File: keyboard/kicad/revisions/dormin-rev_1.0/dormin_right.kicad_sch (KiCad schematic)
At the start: 116 parts, among them J4 Conn_01x06, J5 Conn_01x04, J6 Conn_01x04, Q3 AO3407A, Q4 AO3400A, SW21 SW_Push, SW22 SW_Push, SW23 SW_Push, SW24 SW_Push, SW25 SW_Push, SW26 SW_Push, SW27 SW_Push, SW28 SW_Push, SW29 SW_Push, SW30 SW_Push, SW31 SW_Push, SW32 SW_Push, SW33 SW_Push, SW34 SW_Push, SW35 SW_Push, SW36 SW_Push, SW37 SW_Push, SW38 SW_Push, SW39 SW_Push, SW40 SW_Push, U5 XIAO-nRF52840-Plus-SMD, U6 TPD2E2U06DCK

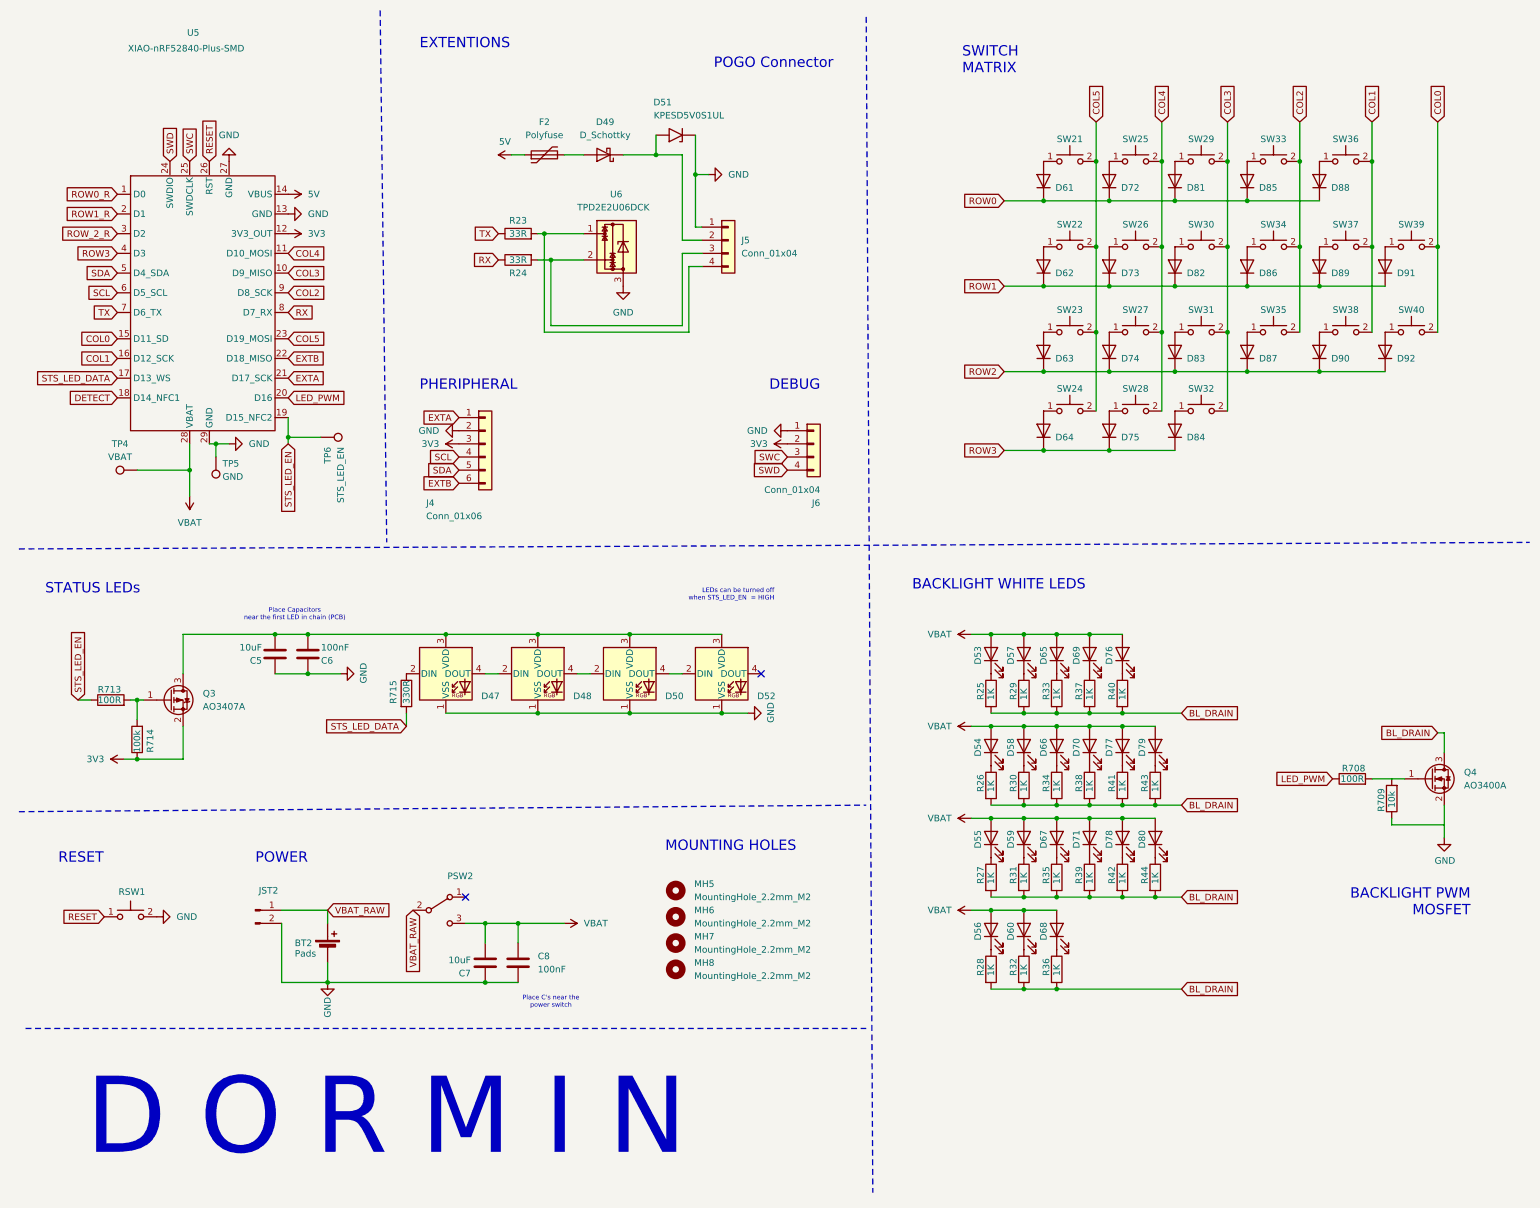
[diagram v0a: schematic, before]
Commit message: chore: update reference names for the right schematic
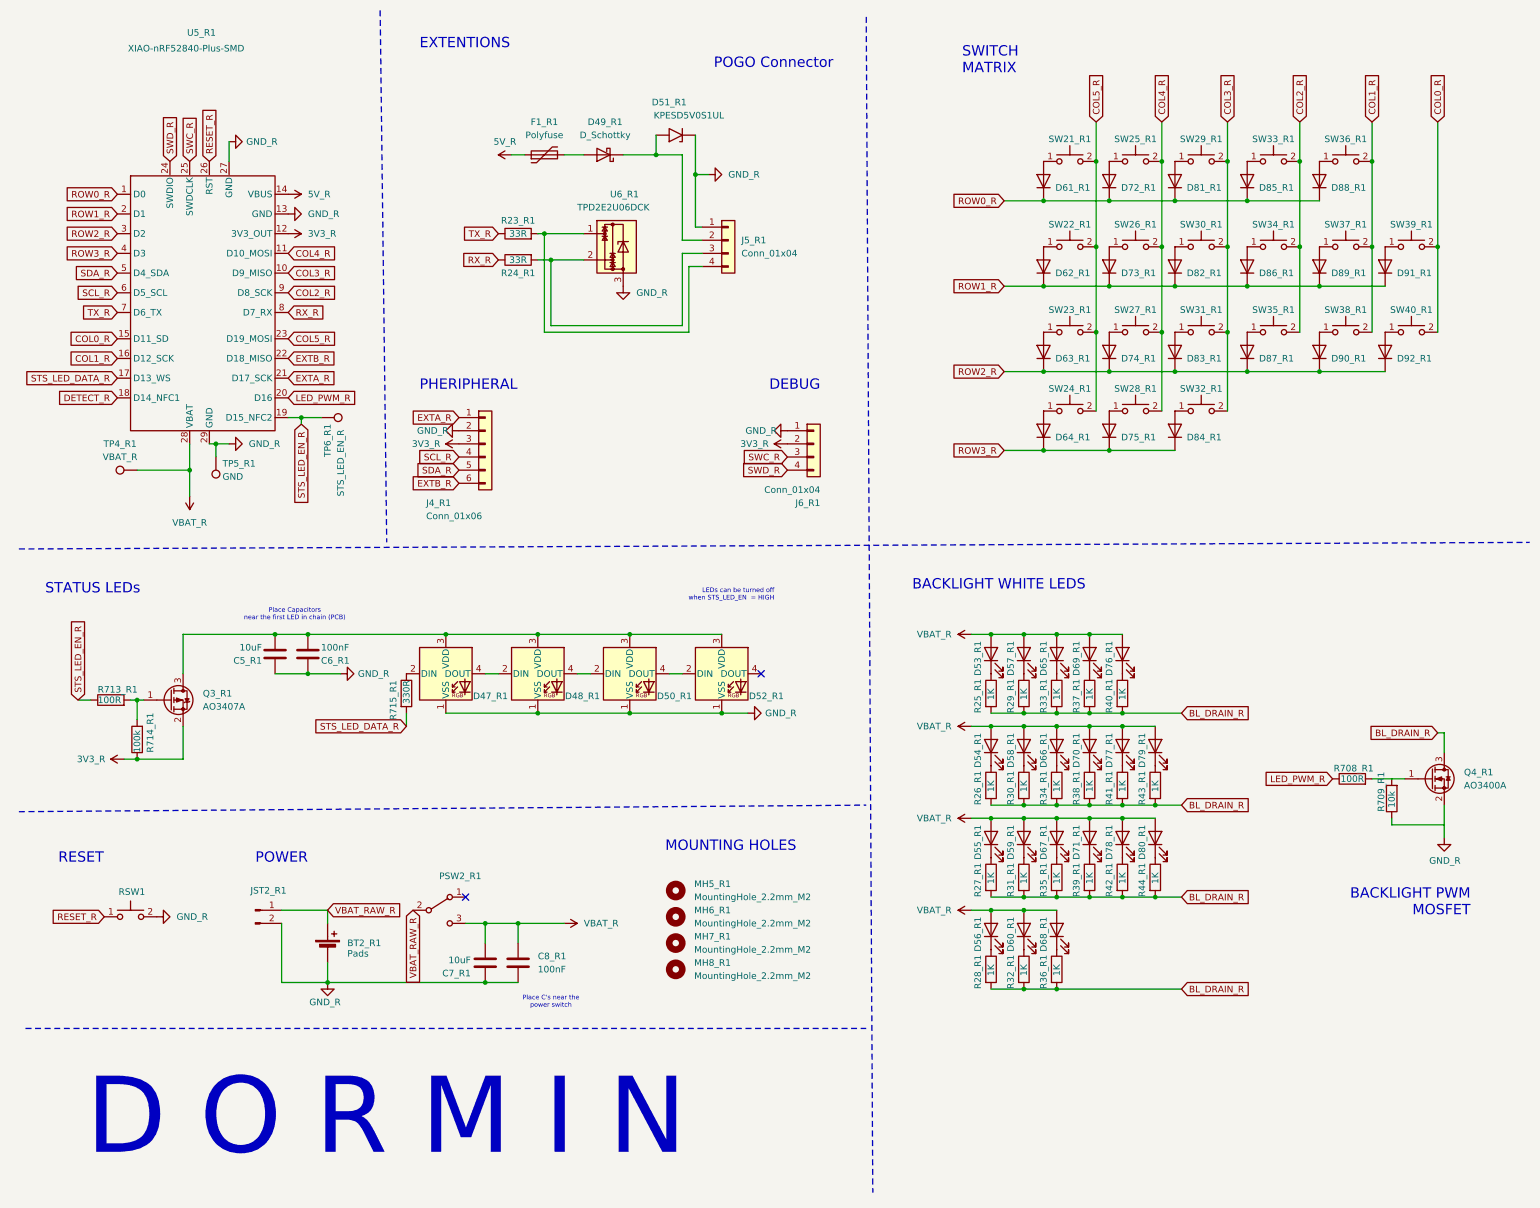
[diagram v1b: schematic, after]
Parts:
- TP4_R1: renamed from TP4; value VBAT -> VBAT_R
- TP6_R1: renamed from TP6; value STS_LED_EN -> STS_LED_EN_R
- renumbered BT2 to BT2_R1, C5 to C5_R1, C6 to C6_R1, C7 to C7_R1, C8 to C8_R1, D47 to D47_R1, D48 to D48_R1, D49 to D49_R1, D50 to D50_R1, D51 to D51_R1, D52 to D52_R1, D53 to D53_R1, D54 to D54_R1, D55 to D55_R1, D56 to D56_R1, D57 to D57_R1, D58 to D58_R1, D59 to D59_R1, D60 to D60_R1, D61 to D61_R1, D62 to D62_R1, D63 to D63_R1, D64 to D64_R1, D65 to D65_R1, D66 to D66_R1, D67 to D67_R1, D68 to D68_R1, D69 to D69_R1, D70 to D70_R1, D71 to D71_R1, D72 to D72_R1, D73 to D73_R1, D74 to D74_R1, D75 to D75_R1, D76 to D76_R1, D77 to D77_R1, D78 to D78_R1, D79 to D79_R1, D80 to D80_R1, D81 to D81_R1, D82 to D82_R1, D83 to D83_R1, D84 to D84_R1, D85 to D85_R1, D86 to D86_R1, D87 to D87_R1, D88 to D88_R1, D89 to D89_R1, D90 to D90_R1, D91 to D91_R1, D92 to D92_R1, F2 to F1_R1, J4 to J4_R1, J5 to J5_R1, J6 to J6_R1, JST2 to JST2_R1, MH5 to MH5_R1, MH6 to MH6_R1, MH7 to MH7_R1, MH8 to MH8_R1, PSW2 to PSW2_R1, Q3 to Q3_R1, Q4 to Q4_R1, R23 to R23_R1, R24 to R24_R1, R25 to R25_R1, R26 to R26_R1, R27 to R27_R1, R28 to R28_R1, R29 to R29_R1, R30 to R30_R1, R31 to R31_R1, R32 to R32_R1, R33 to R33_R1, R34 to R34_R1, R35 to R35_R1, R36 to R36_R1, R37 to R37_R1, R38 to R38_R1, R39 to R39_R1, R40 to R40_R1, R41 to R41_R1, R42 to R42_R1, R43 to R43_R1, R44 to R44_R1, R708 to R708_R1, R709 to R709_R1, R713 to R713_R1, R714 to R714_R1, R715 to R715_R1, RSW2 to RSW2_R1, SW21 to SW21_R1, SW22 to SW22_R1, SW23 to SW23_R1, SW24 to SW24_R1, SW25 to SW25_R1, SW26 to SW26_R1, SW27 to SW27_R1, SW28 to SW28_R1, SW29 to SW29_R1, SW30 to SW30_R1, SW31 to SW31_R1, SW32 to SW32_R1, SW33 to SW33_R1, SW34 to SW34_R1, SW35 to SW35_R1, SW36 to SW36_R1, SW37 to SW37_R1, SW38 to SW38_R1, SW39 to SW39_R1, SW40 to SW40_R1, TP5 to TP5_R1, U5 to U5_R1, U6 to U6_R1
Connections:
- net ROW0 is gone; now on net ROW0_R: D61_R1.1 (K), D72_R1.1 (K), D81_R1.1 (K), D85_R1.1 (K), D88_R1.1 (K)
- net ROW1 is gone; now on net ROW1_R: D62_R1.1 (K), D73_R1.1 (K), D82_R1.1 (K), D86_R1.1 (K), D89_R1.1 (K), D91_R1.1 (K)
- net ROW_2_R is gone; now on net ROW2_R: U5_R1.3 (D2)
- net 3V3 renamed 3V3_R
- net 5V renamed 5V_R
- net BL_DRAIN renamed BL_DRAIN_R
- net COL0 renamed COL0_R
- net COL1 renamed COL1_R
- net COL2 renamed COL2_R
- net COL3 renamed COL3_R
- net COL4 renamed COL4_R
- net COL5 renamed COL5_R
- net DETECT renamed DETECT_R
- net EXTA renamed EXTA_R
- net EXTB renamed EXTB_R
- net GND renamed GND_R
- net LED_PWM renamed LED_PWM_R
- net RESET renamed RESET_R
- net ROW2 renamed ROW2_R
- net ROW3 renamed ROW3_R
- net RX renamed RX_R
- net SCL renamed SCL_R
- net SDA renamed SDA_R
- net STS_LED_DATA renamed STS_LED_DATA_R
- net STS_LED_EN renamed STS_LED_EN_R
- net SWC renamed SWC_R
- net SWD renamed SWD_R
- net TX renamed TX_R
- net VBAT renamed VBAT_R
- net VBAT_RAW renamed VBAT_RAW_R
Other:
- moved on the sheet: TP6_R1

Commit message: feat: updated pogo-pin schematics
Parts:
- removed D49_R1: D_Schottky, Diode_SMD:D_SOD-523, symbol Device:D_Schottky
- removed D51_R1: KPESD5V0S1UL, Diode_SMD:D_SOD-882, symbol Diode:SMF5V0A
- removed F1_R1: Polyfuse, Fuse:Fuse_1206_3216Metric, symbol Device:Polyfuse
- removed J5_R1: Conn_01x04, willkeebs_misc:SMD_Conn_1x04_P2.54mm_Vertical, symbol Connector_Generic:Conn_01x04
- removed R23_R1, R24_R1: 33R, Resistor_SMD:R_0603_1608Metric, symbol Device:R
- removed U6_R1: TPD2E2U06DCK, Package_TO_SOT_SMD:SOT-323_SC-70, symbol Power_Protection:TPD2E2U06DCK
- added D47_R: D_Schottky, Diode_SMD:D_SOD-523, symbol Device:D_Schottky
- added D48_R: KPESD5V0S1UL, Diode_SMD:D_SOD-882, symbol Diode:SMF5V0A
- added F2_R: Polyfuse, Fuse:Fuse_1206_3216Metric, symbol Device:Polyfuse
- added J4_R: Conn_01x02, symbol Connector_Generic:Conn_01x02
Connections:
- net 5V_R: now also F2_R.1
- net GND_R: now also D48_R.1 (A1), J4_R.1 (Pin_1)
- net RX_R: no longer names the net of U5_R1.8 (D7_RX)
- net TX_R: no longer names the net of U5_R1.7 (D6_TX)
- new net: D47_R.1 (K), D48_R.2 (A2), J4_R.2 (Pin_2)
- new net: D47_R.2 (A), F2_R.2
- no-connect marks 2 -> 4
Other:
- note added: "POGO (Charging Only)"
- note removed: "EXTENTIONS"
- note removed: "POGO Connector"
- moved on the sheet: J4_R1, J6_R1

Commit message: feat: added initial components to the right places
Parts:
- J4_R2: renamed from J4_R; footprint (none) -> willkeebs_misc:SMD_Conn_1x02_P2.54mm_Vertical
- renumbered D47_R to D47_R2, D48_R to D48_R2, F2_R to F2_R1, SW21_R1 to SW21, SW22_R1 to SW22, SW23_R1 to SW23, SW24_R1 to SW24, SW25_R1 to SW25, SW26_R1 to SW26, SW27_R1 to SW27, SW28_R1 to SW28, SW29_R1 to SW29, SW30_R1 to SW30, SW31_R1 to SW31, SW32_R1 to SW32, SW33_R1 to SW33, SW34_R1 to SW34, SW35_R1 to SW35, SW36_R1 to SW36, SW37_R1 to SW37, SW38_R1 to SW38, SW39_R1 to SW39, SW40_R1 to SW40
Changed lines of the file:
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@@
 		(in_pos_files yes)
 		(dnp no)
-		(property "Reference" "SW34_R1"
+		(property "Reference" "SW34"
 			(at 255.27 54.102 0)
 			(show_name no)
@@
 			(project "dormin"
 				(path "/603afaa0-4142-4673-b835-76ba767ab9eb/c34ad971-40ee-4ba1-b588-4be495453fb3"
-					(reference "SW34_R1")
+					(reference "SW34")
 					(unit 1)
 				)
@@
 		(in_pos_files yes)
 		(dnp no)
-		(property "Reference" "SW27_R1"
+		(property "Reference" "SW27"
 			(at 228.6 70.612 0)
 			(show_name no)
@@
 			(project "dormin"
 				(path "/603afaa0-4142-4673-b835-76ba767ab9eb/c34ad971-40ee-4ba1-b588-4be495453fb3"
-					(reference "SW27_R1")
+					(reference "SW27")
 					(unit 1)
 				)
@@
 		(in_pos_files yes)
 		(dnp no)
-		(property "Reference" "SW38_R1"
+		(property "Reference" "SW38"
 			(at 269.24 70.612 0)
 			(show_name no)
@@
 			(project "dormin"
 				(path "/603afaa0-4142-4673-b835-76ba767ab9eb/c34ad971-40ee-4ba1-b588-4be495453fb3"
-					(reference "SW38_R1")
+					(reference "SW38")
 					(unit 1)
 				)
@@
 		(in_pos_files yes)
 		(dnp no)
-		(property "Reference" "SW23_R1"
+		(property "Reference" "SW23"
 			(at 215.9 70.612 0)
 			(show_name no)
@@
 			(project "dormin"
 				(path "/603afaa0-4142-4673-b835-76ba767ab9eb/c34ad971-40ee-4ba1-b588-4be495453fb3"
-					(reference "SW23_R1")
+					(reference "SW23")
 					(unit 1)
 				)
@@
 		(dnp no)
 		(fields_autoplaced yes)
-		(property "Reference" "#PWR013_E"
+		(property "Reference" "#PWR013_E01"
 			(at 135.89 31.75 0)
 			(hide yes)
@@
 			(project "dormin"
 				(path "/603afaa0-4142-4673-b835-76ba767ab9eb/c34ad971-40ee-4ba1-b588-4be495453fb3"
-					(reference "#PWR013_E")
+					(reference "#PWR013_E01")
 					(unit 1)
 				)
@@
 		(in_pos_files yes)
 		(dnp no)
-		(property "Reference" "SW26_R1"
+		(property "Reference" "SW26"
 			(at 228.6 54.102 0)
 			(show_name no)
@@
 			(project "dormin"
 				(path "/603afaa0-4142-4673-b835-76ba767ab9eb/c34ad971-40ee-4ba1-b588-4be495453fb3"
-					(reference "SW26_R1")
+					(reference "SW26")
 					(unit 1)
 				)
@@
 		(dnp no)
 		(fields_autoplaced yes)
-		(property "Reference" "#PWR019_R"
+		(property "Reference" "#PWR019_R02"
 			(at 97.79 45.72 0)
 			(hide yes)
@@
 			(project "dormin"
 				(path "/603afaa0-4142-4673-b835-76ba767ab9eb/c34ad971-40ee-4ba1-b588-4be495453fb3"
-					(reference "#PWR019_R")
+					(reference "#PWR019_R02")
 					(unit 1)
 				)
@@
 		(dnp no)
 		(fields_autoplaced yes)
-		(property "Reference" "J4_R"
+		(property "Reference" "J4_R2"
 			(at 138.43 43.1799 0)
 			(show_name no)
@@
 			)
 		)
-		(property "Footprint" ""
+		(property "Footprint" "willkeebs_misc:SMD_Conn_1x02_P2.54mm_Vertical"
 			(at 135.89 43.18 0)
 			(hide yes)
@@
 			(project "dormin"
 				(path "/603afaa0-4142-4673-b835-76ba767ab9eb/c34ad971-40ee-4ba1-b588-4be495453fb3"
-					(reference "J4_R")
+					(reference "J4_R2")
 					(unit 1)
 				)
@@
 		(in_pos_files yes)
 		(dnp no)
-		(property "Reference" "SW30_R1"
+		(property "Reference" "SW30"
 			(at 241.3 54.102 0)
 			(show_name no)
@@
 			(project "dormin"
 				(path "/603afaa0-4142-4673-b835-76ba767ab9eb/c34ad971-40ee-4ba1-b588-4be495453fb3"
-					(reference "SW30_R1")
+					(reference "SW30")
 					(unit 1)
 				)
@@
 		(in_pos_files yes)
 		(dnp no)
-		(property "Reference" "SW31_R1"
+		(property "Reference" "SW31"
 			(at 241.3 70.612 0)
 			(show_name no)
@@
 			(project "dormin"
 				(path "/603afaa0-4142-4673-b835-76ba767ab9eb/c34ad971-40ee-4ba1-b588-4be495453fb3"
-					(reference "SW31_R1")
+					(reference "SW31")
 					(unit 1)
 				)
@@
 		(in_pos_files yes)
 		(dnp no)
-		(property "Reference" "SW24_R1"
+		(property "Reference" "SW24"
 			(at 215.9 85.852 0)
 			(show_name no)
@@
 			(project "dormin"
 				(path "/603afaa0-4142-4673-b835-76ba767ab9eb/c34ad971-40ee-4ba1-b588-4be495453fb3"
-					(reference "SW24_R1")
+					(reference "SW24")
 					(unit 1)
 				)
@@
 		(in_pos_files yes)
 		(dnp no)
-		(property "Reference" "SW29_R1"
+		(property "Reference" "SW29"
 			(at 241.3 37.592 0)
 			(show_name no)
@@
 			(project "dormin"
 				(path "/603afaa0-4142-4673-b835-76ba767ab9eb/c34ad971-40ee-4ba1-b588-4be495453fb3"
-					(reference "SW29_R1")
+					(reference "SW29")
 					(unit 1)
 				)
@@
 		(in_pos_files yes)
 		(dnp no)
-		(property "Reference" "D48_R"
+		(property "Reference" "D48_R2"
 			(at 116.84 35.56 0)
 			(show_name no)
@@
 			(project "dormin"
 				(path "/603afaa0-4142-4673-b835-76ba767ab9eb/c34ad971-40ee-4ba1-b588-4be495453fb3"
-					(reference "D48_R")
+					(reference "D48_R2")
 					(unit 1)
 				)
@@
 		(in_pos_files yes)
 		(dnp no)
-		(property "Reference" "D47_R"
+		(property "Reference" "D47_R2"
 			(at 111.76 48.26 0)
 			(show_name no)
@@
 			(project "dormin"
 				(path "/603afaa0-4142-4673-b835-76ba767ab9eb/c34ad971-40ee-4ba1-b588-4be495453fb3"
-					(reference "D47_R")
+					(reference "D47_R2")
 					(unit 1)
 				)
@@
 		(in_pos_files yes)
 		(dnp no)
-		(property "Reference" "SW21_R1"
+		(property "Reference" "SW21"
 			(at 215.9 37.592 0)
 			(show_name no)
@@
 			(project "dormin"
 				(path "/603afaa0-4142-4673-b835-76ba767ab9eb/c34ad971-40ee-4ba1-b588-4be495453fb3"
-					(reference "SW21_R1")
+					(reference "SW21")
 					(unit 1)
 				)
@@
 		(in_pos_files yes)
 		(dnp no)
-		(property "Reference" "SW37_R1"
+		(property "Reference" "SW37"
 			(at 269.24 54.102 0)
 			(show_name no)
@@
 			(project "dormin"
 				(path "/603afaa0-4142-4673-b835-76ba767ab9eb/c34ad971-40ee-4ba1-b588-4be495453fb3"
-					(reference "SW37_R1")
+					(reference "SW37")
 					(unit 1)
 				)
@@
 		(in_pos_files yes)
 		(dnp no)
-		(property "Reference" "SW35_R1"
+		(property "Reference" "SW35"
 			(at 255.27 70.612 0)
 			(show_name no)
@@
 			(project "dormin"
 				(path "/603afaa0-4142-4673-b835-76ba767ab9eb/c34ad971-40ee-4ba1-b588-4be495453fb3"
-					(reference "SW35_R1")
+					(reference "SW35")
 					(unit 1)
 				)
@@
 		(in_pos_files yes)
 		(dnp no)
-		(property "Reference" "SW40_R1"
+		(property "Reference" "SW40"
 			(at 281.94 70.612 0)
 			(show_name no)
@@
 			(project "dormin"
 				(path "/603afaa0-4142-4673-b835-76ba767ab9eb/c34ad971-40ee-4ba1-b588-4be495453fb3"
-					(reference "SW40_R1")
+					(reference "SW40")
 					(unit 1)
 				)
@@
 		(in_pos_files yes)
 		(dnp no)
-		(property "Reference" "SW25_R1"
+		(property "Reference" "SW25"
 			(at 228.6 37.592 0)
 			(show_name no)
@@
 			(project "dormin"
 				(path "/603afaa0-4142-4673-b835-76ba767ab9eb/c34ad971-40ee-4ba1-b588-4be495453fb3"
-					(reference "SW25_R1")
+					(reference "SW25")
 					(unit 1)
 				)
@@
 		(in_pos_files yes)
 		(dnp no)
-		(property "Reference" "SW32_R1"
+		(property "Reference" "SW32"
 			(at 241.3 85.852 0)
 			(show_name no)
@@
 			(project "dormin"
 				(path "/603afaa0-4142-4673-b835-76ba767ab9eb/c34ad971-40ee-4ba1-b588-4be495453fb3"
-					(reference "SW32_R1")
+					(reference "SW32")
 					(unit 1)
 				)
@@
 		(in_pos_files yes)
 		(dnp no)
-		(property "Reference" "SW22_R1"
+		(property "Reference" "SW22"
 			(at 215.9 54.102 0)
 			(show_name no)
@@
 			(project "dormin"
 				(path "/603afaa0-4142-4673-b835-76ba767ab9eb/c34ad971-40ee-4ba1-b588-4be495453fb3"
-					(reference "SW22_R1")
+					(reference "SW22")
 					(unit 1)
 				)
@@
 		(in_pos_files yes)
 		(dnp no)
-		(property "Reference" "SW39_R1"
+		(property "Reference" "SW39"
 			(at 281.94 54.102 0)
 			(show_name no)
@@
 			(project "dormin"
 				(path "/603afaa0-4142-4673-b835-76ba767ab9eb/c34ad971-40ee-4ba1-b588-4be495453fb3"
-					(reference "SW39_R1")
+					(reference "SW39")
 					(unit 1)
 				)
@@
 		(in_pos_files yes)
 		(dnp no)
-		(property "Reference" "SW36_R1"
+		(property "Reference" "SW36"
 			(at 269.24 37.592 0)
 			(show_name no)
@@
 			(project "dormin"
 				(path "/603afaa0-4142-4673-b835-76ba767ab9eb/c34ad971-40ee-4ba1-b588-4be495453fb3"
-					(reference "SW36_R1")
+					(reference "SW36")
 					(unit 1)
 				)
@@
 		(in_pos_files yes)
 		(dnp no)
-		(property "Reference" "F2_R"
+		(property "Reference" "F2_R1"
 			(at 100.33 48.26 90)
 			(show_name no)
@@
 			(project "dormin"
 				(path "/603afaa0-4142-4673-b835-76ba767ab9eb/c34ad971-40ee-4ba1-b588-4be495453fb3"
-					(reference "F2_R")
+					(reference "F2_R1")
 					(unit 1)
 				)
@@
 		(in_pos_files yes)
 		(dnp no)
-		(property "Reference" "SW28_R1"
+		(property "Reference" "SW28"
 			(at 228.6 85.852 0)
 			(show_name no)
@@
 			(project "dormin"
 				(path "/603afaa0-4142-4673-b835-76ba767ab9eb/c34ad971-40ee-4ba1-b588-4be495453fb3"
-					(reference "SW28_R1")
+					(reference "SW28")
 					(unit 1)
 				)
@@
 		(in_pos_files yes)
 		(dnp no)
-		(property "Reference" "SW33_R1"
+		(property "Reference" "SW33"
 			(at 255.27 37.592 0)
 			(show_name no)
@@
 			(project "dormin"
 				(path "/603afaa0-4142-4673-b835-76ba767ab9eb/c34ad971-40ee-4ba1-b588-4be495453fb3"
-					(reference "SW33_R1")
+					(reference "SW33")
 					(unit 1)
 				)
